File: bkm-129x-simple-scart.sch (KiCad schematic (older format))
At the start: 53 parts, among them J1 SCART-F, J2 RCA-RA, J5 Conn_02x32_Row_Letter_Last, Q1 DTC144EKA, U1 ADG1611, U2 THS7374, U3 arduino-nano-v3, U4 74LVC125, U5 MIC3490-3.3

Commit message: Fixed some footprints
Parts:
- added J3: RIGHT, rcj-41x:RCJ-04X, symbol Conn_Coaxial
- J2: value RCA-RA -> LEFT
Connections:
- net AUDIO_R: now also J3.1 (In)
- net GND: now also J3.2 (Ext)
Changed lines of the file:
@@
 P 6500 1250
 F 0 "J2" H 6510 1370 50  0000 C CNN
-F 1 "RCA-RA" V 6615 1250 50  0000 C CNN
+F 1 "LEFT" V 6615 1250 50  0000 C CNN
 F 2 "rcj-41x:RCJ-04X" H 6500 1250 50  0001 C CNN
 F 3 "" H 6500 1250 50  0001 C CNN
@@
 	1    0    0    -1
 $EndComp
+$Comp
+L Conn_Coaxial J3
+U 1 1 5E56D5E0
+P 7350 1250
+F 0 "J3" H 7360 1370 50  0000 C CNN
+F 1 "RIGHT" V 7465 1250 50  0000 C CNN
+F 2 "rcj-41x:RCJ-04X" H 7350 1250 50  0001 C CNN
+F 3 "" H 7350 1250 50  0001 C CNN
+	1    7350 1250
+	1    0    0    -1
+$EndComp
+$Comp
+L GNDA #PWR072
+U 1 1 5E56D99C
+P 7350 1450
+F 0 "#PWR072" H 7350 1200 50  0001 C CNN
+F 1 "GNDA" H 7350 1300 50  0000 C CNN
+F 2 "" H 7350 1450 50  0001 C CNN
+F 3 "" H 7350 1450 50  0001 C CNN
+	1    7350 1450
+	1    0    0    -1
+$EndComp
+Text Label 7200 1250 2    60   ~ 0
+AUDIO_R
 $EndSCHEMATC

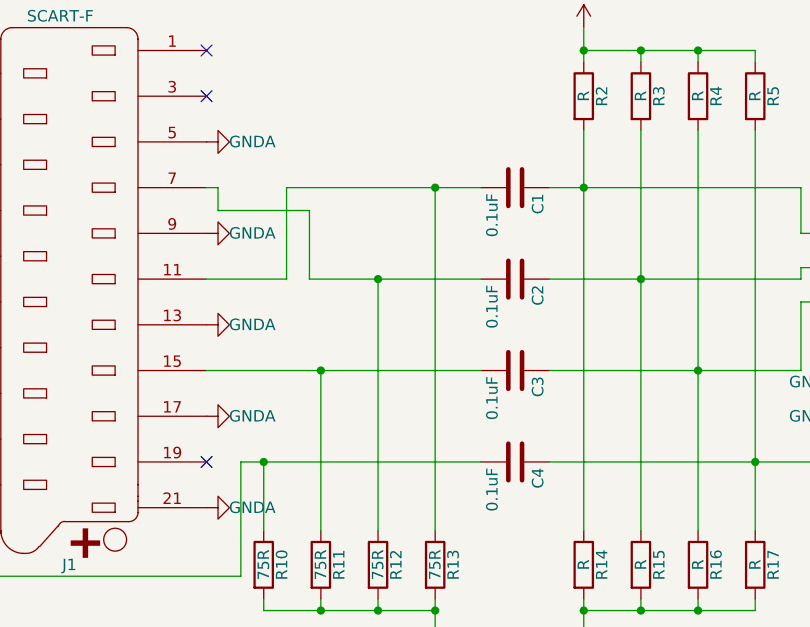
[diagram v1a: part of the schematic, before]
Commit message: Fixed SCART pad size and added signal names
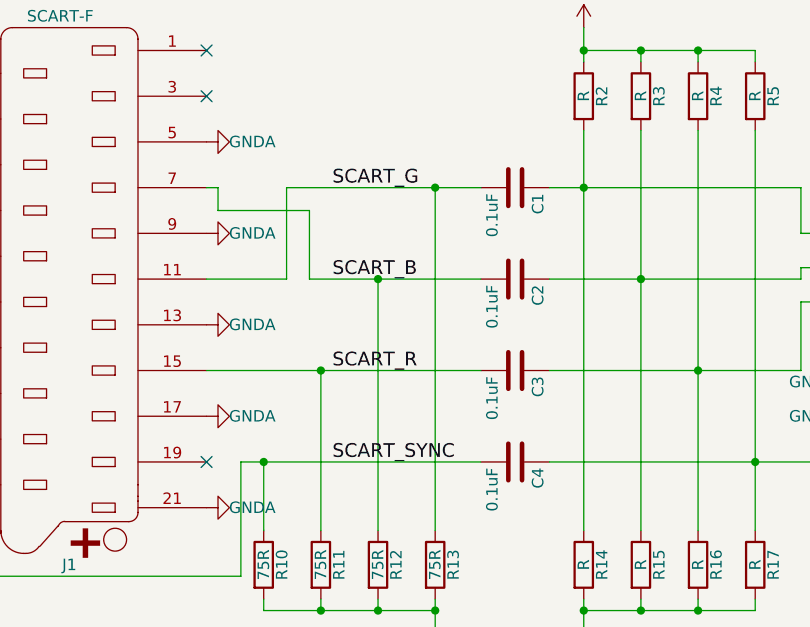
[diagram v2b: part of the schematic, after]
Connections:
- net SCART_G: now reaches C1.2, J1.11 (P11), R13.1
- net SCART_R: now reaches C3.2, J1.15 (P15), R11.1
- net SCART_B: now reaches C2.2, J1.7 (P7), R12.1
- net SCART_SYNC: now reaches C4.2, J1.20 (P20), R10.1
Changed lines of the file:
@@
 Text Label 7200 1250 2    60   ~ 0
 AUDIO_R
+Text Label 2700 2400 0    60   ~ 0
+SCART_B
+Text Label 2700 2000 0    60   ~ 0
+SCART_G
+Text Label 2700 2800 0    60   ~ 0
+SCART_R
+Text Label 2700 3200 0    60   ~ 0
+SCART_SYNC
 $EndSCHEMATC

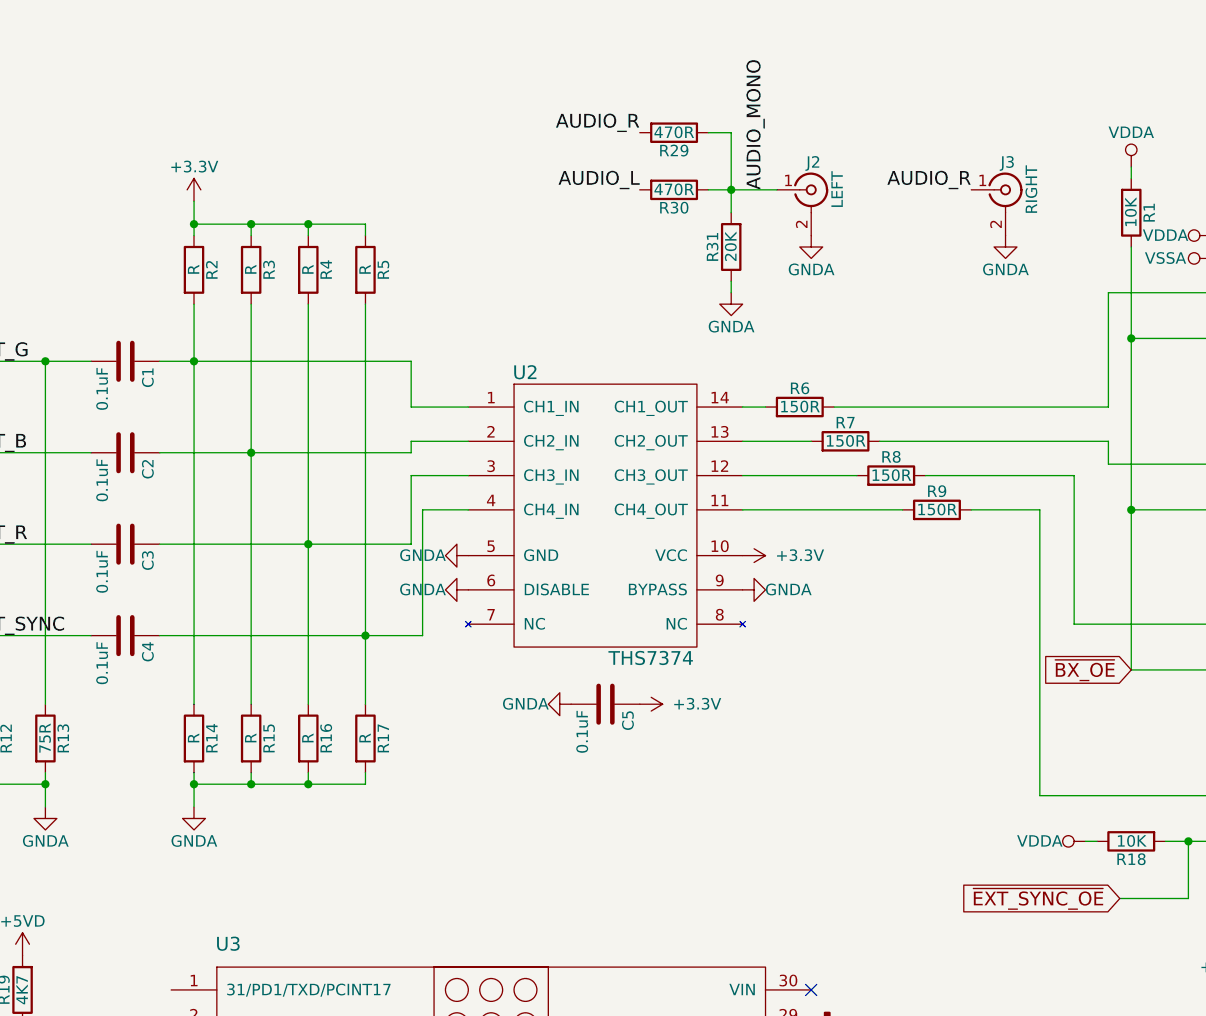
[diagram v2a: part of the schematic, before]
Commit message: Added audio switch, enlarge holes for SCART fasteners
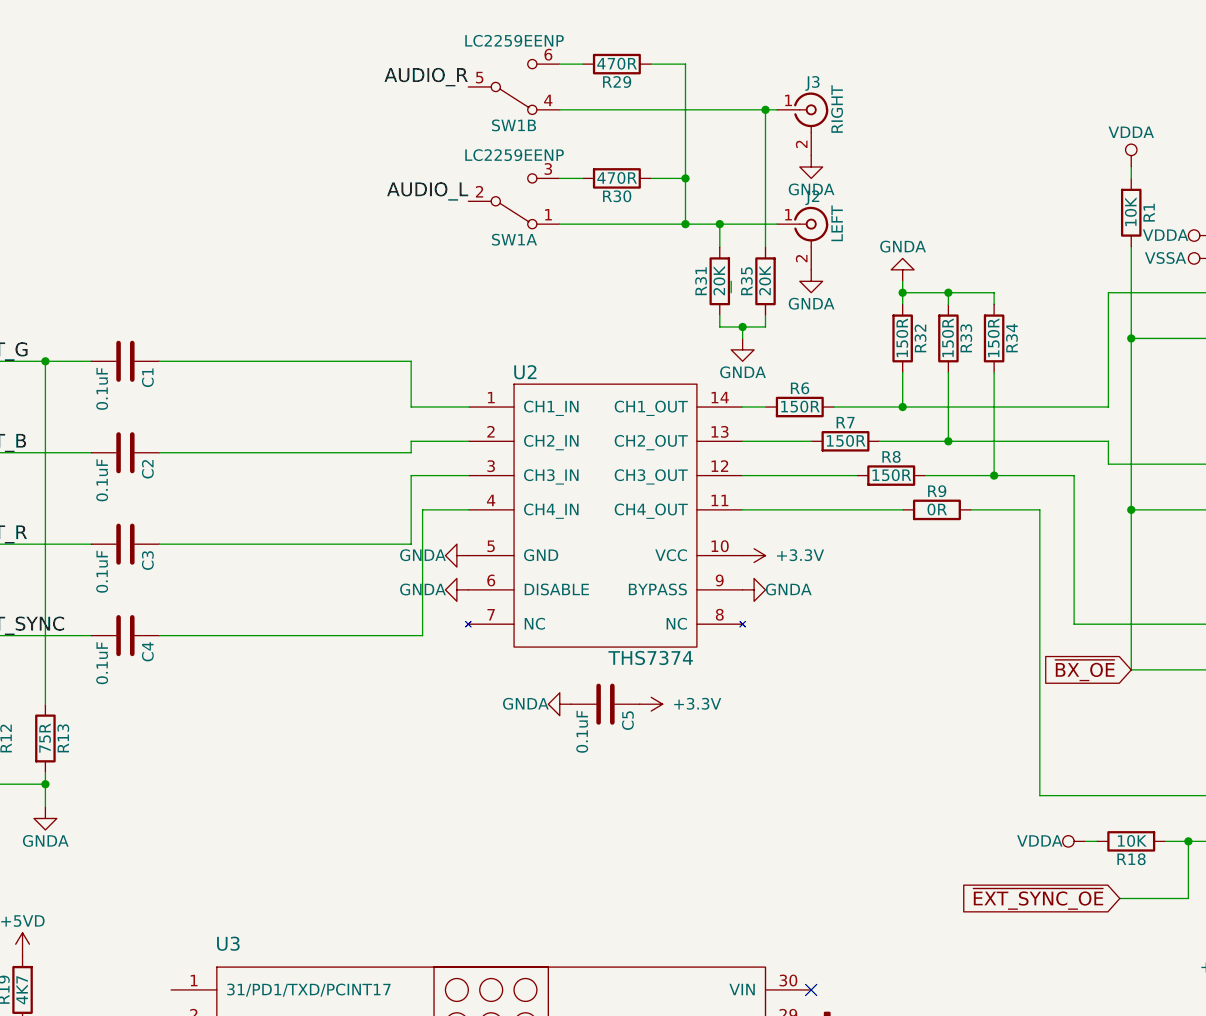
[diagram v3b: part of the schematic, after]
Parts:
- removed R14, R15, R16, R17, R2, R3, R4, R5: R, Resistors_SMD:R_0805_HandSoldering, symbol R
- added R32, R33, R34: 150R, Resistors_SMD:R_0805_HandSoldering, symbol R
- added R35: 20K, Resistors_SMD:R_0805_HandSoldering, symbol R
- added SW1: LC2259EENP, LC2259:LC2259, symbol SW_DPDT_x2
- R9: value 150R -> 0R
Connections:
- net AUDIO_L: now also SW1.2 (B); no longer R30.2
- net AUDIO_R: now also SW1.5 (B); no longer J3.1 (In), R29.2
- net GND: now also R32.2, R33.2, R34.2, R35.1
- net at R6.1, U1.6 (S): now also R32.1
- net at R7.1, U1.3 (S): now also R33.1
- net at R8.1, U1.11 (S): now also R34.1
- net AUDIO_MONO: no longer names the net of J2.1 (In), R29.1, R30.1, R31.2
- net AUDIO_MONO: now also SW1.1 (A)
- new net: R30.2, SW1.3 (C)
- new net: R29.2, SW1.6 (C)
- new net: J3.1 (In), R35.2, SW1.4 (A)

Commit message: Revision B
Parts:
- C1, C10, C11, C12, C2, C3, C4, C5, C6, C9: symbol C -> bkm-129x-simple-scart-rescue:C
- C13, C7, C8: symbol CP -> bkm-129x-simple-scart-rescue:CP
- J1: symbol SCART-F -> bkm-129x-simple-scart-rescue:SCART-F
- J2, J3: symbol Conn_Coaxial -> bkm-129x-simple-scart-rescue:Conn_Coaxial
- J5: symbol Conn_02x32_Row_Letter_Last -> bkm-129x-simple-scart-rescue:Conn_02x32_Row_Letter_Last
- Q1: symbol DTC144EKA -> dtc144eka:DTC144EKA
- R1, R10, R11, R12, R13, R18, R19, R20, R21, R22, R23, R24, R25, R26, R27, R28, R29, R30, R31, R32, R33, R34, R35, R6, R7, R8, R9: symbol R -> bkm-129x-simple-scart-rescue:R
- SW1: symbol SW_DPDT_x2 -> bkm-129x-simple-scart-rescue:SW_DPDT_x2
- U1: symbol ADG1611 -> adg1611:ADG1611
- U2: symbol THS7374 -> ths7374:THS7374
- U3: symbol arduino-nano-v3 -> arduino-nano-v3:arduino-nano-v3
- U4: symbol 74LVC125 -> bkm-129x-simple-scart-rescue:74LVC125
- U5: symbol MIC3490 -> mic3490:MIC3490
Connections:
- net +3V3: now also U2.9 (BYPASS)
- net GND: no longer U2.9 (BYPASS)
